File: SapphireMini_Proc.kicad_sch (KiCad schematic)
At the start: 38 parts, among them J801 USB_B_Micro, J802 Conn_02x05_Odd_Even, J803 Conn_02x05_Odd_Even, J805 Conn_01x04_Male, SW801 EVQP7C01P, U801 ATSAMD21G18A-A

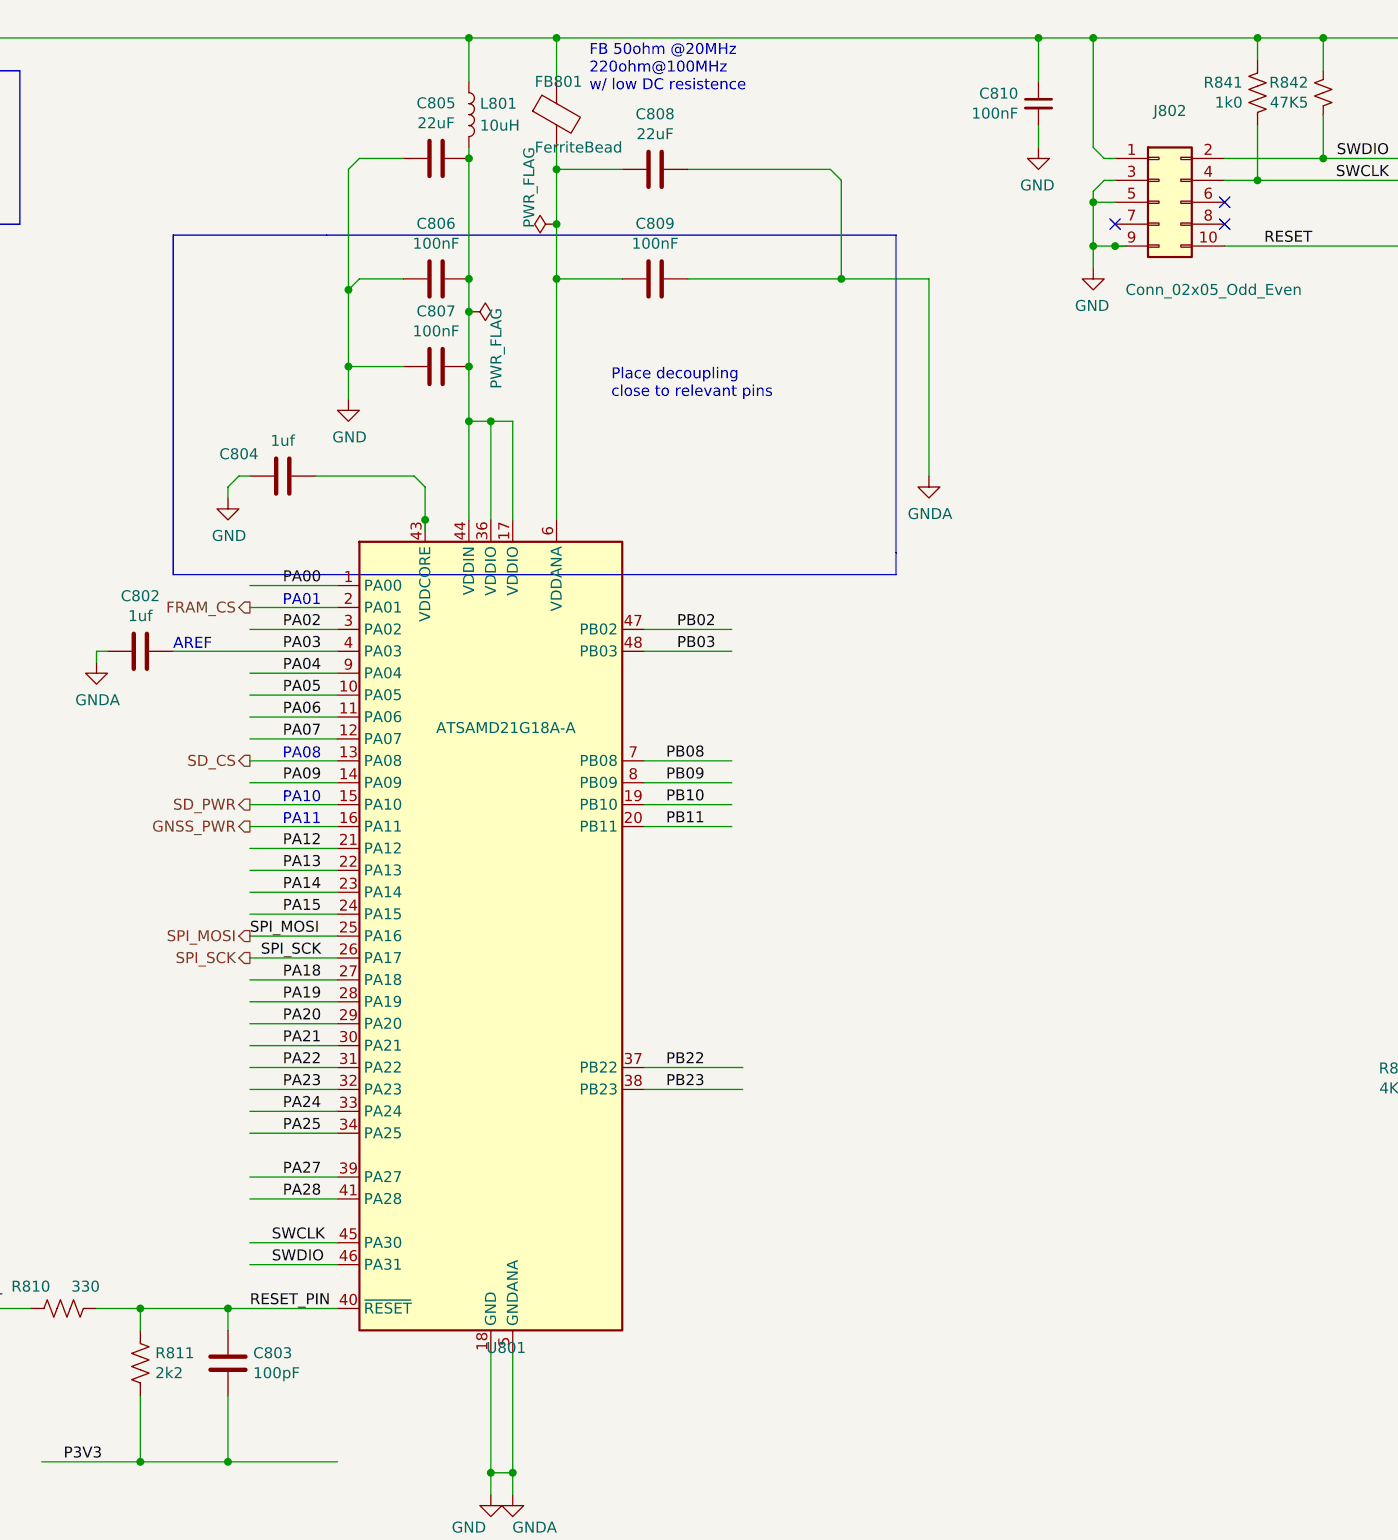
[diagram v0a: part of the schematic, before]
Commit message: Clean PCB but Added new clock to schematic
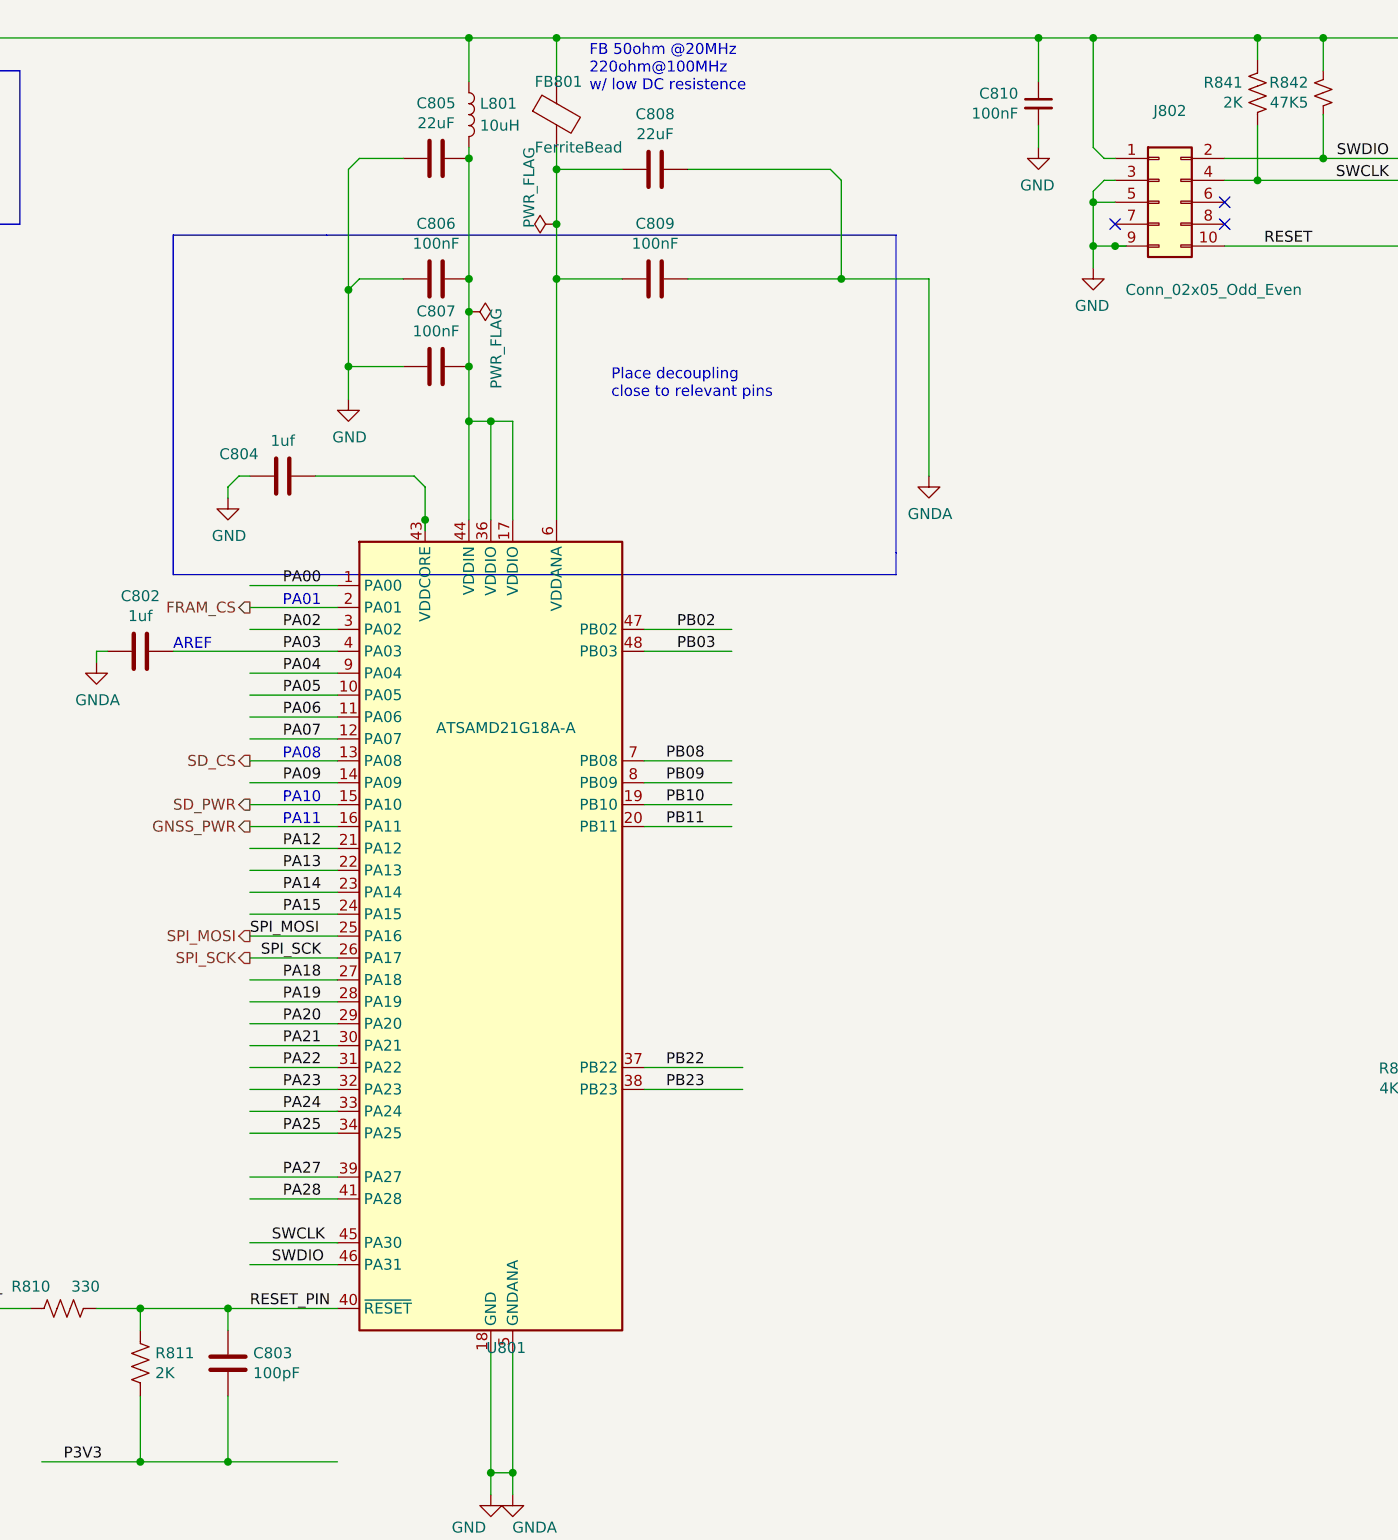
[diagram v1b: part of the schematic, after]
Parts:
- R811: value 2k2 -> 2K; MPN (none) -> CRCW06032K00FKEAC; Manufacturer (none) -> Vishay
- R841: value 1k0 -> 2K; MPN (none) -> CRCW06032K00FKEAC; Manufacturer (none) -> Vishay
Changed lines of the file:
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@@
       (effects (font (size 1.27 1.27)) (justify left))
     )
-    (property "Value" "2k2" (id 1) (at 123.6472 171.323 0)
+    (property "Value" "2K" (id 1) (at 123.6472 171.323 0)
       (effects (font (size 1.27 1.27)) (justify left))
     )
@@
     )
     (property "Datasheet" "~" (id 3) (at 121.92 170.18 0)
+      (effects (font (size 1.27 1.27)) hide)
+    )
+    (property "MPN" "CRCW06032K00FKEAC" (id 4) (at 121.92 170.18 0)
+      (effects (font (size 1.27 1.27)) hide)
+    )
+    (property "Manufacturer" "Vishay" (id 5) (at 121.92 170.18 0)
       (effects (font (size 1.27 1.27)) hide)
     )
@@
       (effects (font (size 1.27 1.27)) (justify left))
     )
-    (property "Value" "1k0" (id 1) (at 249.7328 24.003 0)
+    (property "Value" "2K" (id 1) (at 249.7328 24.003 0)
       (effects (font (size 1.27 1.27)) (justify left))
     )
@@
       (effects (font (size 1.27 1.27)) hide)
     )
+    (property "MPN" "CRCW06032K00FKEAC" (id 4) (at 251.46 22.86 0)
+      (effects (font (size 1.27 1.27)) hide)
+    )
+    (property "Manufacturer" "Vishay" (id 5) (at 251.46 22.86 0)
+      (effects (font (size 1.27 1.27)) hide)
+    )

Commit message: Updating for parts avail
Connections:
- net AUX1: now also R809.4; no longer R812.8
- net PB1: now also R812.5; no longer R809.1
- net RS232_RXD5: now also R812.8; no longer R812.6
- net RS232_TXD5: now also R812.7; no longer R812.5
- net SD_CD: now also R809.1; no longer R812.7
- net VBAT_MON: now also R812.6; no longer R809.4
- net AUX3 renamed CLK_EVI
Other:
- note added: "Attn"
- note added: "Aux Connector"
- note added: "Debug Connector"
- note added: "Processor"
- moved on the sheet: C801, C802, C803, C804, C805, C806, C807, C808, C809, C810, CR801, D801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

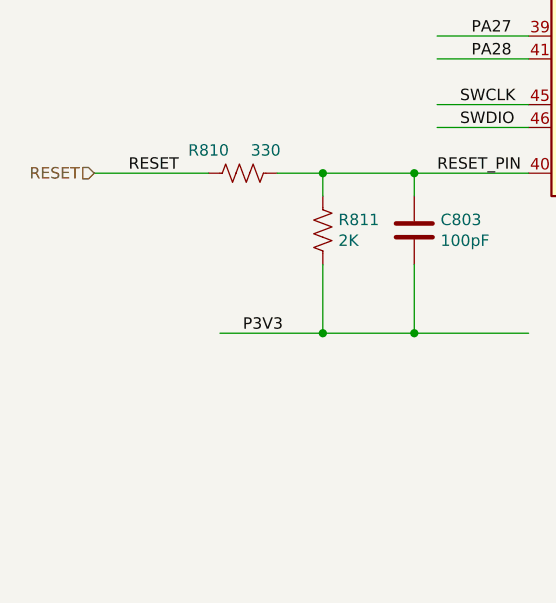
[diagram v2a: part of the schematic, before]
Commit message: Skematic updated for power and 1PSI sensor
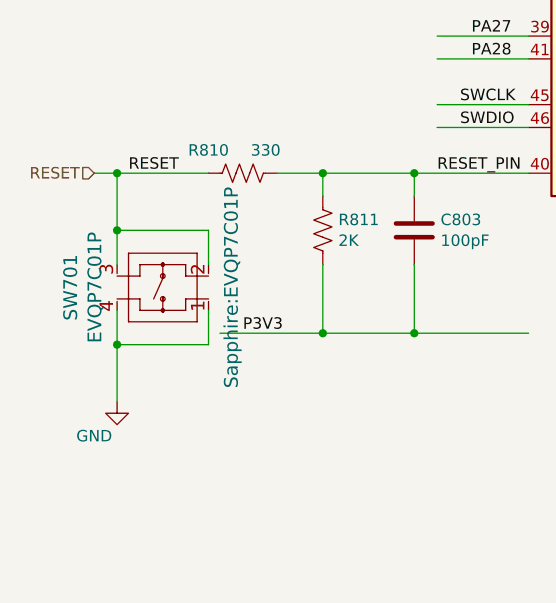
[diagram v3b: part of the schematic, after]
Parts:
- added SW701: EVQP7C01P, Sapphire:EVQP7C01P, symbol EVQP7C01P:EVQP7C01P
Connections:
- net GND: now also SW701.1, SW701.4
- net RESET: now also SW701.2, SW701.3
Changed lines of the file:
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@@
   (junction (at 217.17 81.28) (diameter 0) (color 0 0 0 0)
   )
+  (junction (at 26.67 209.55) (diameter 0) (color 0 0 0 0)
+  )
   (junction (at 49.53 208.28) (diameter 0) (color 0 0 0 0)
   )
@@
   (junction (at 200.66 105.41) (diameter 0) (color 0 0 0 0)
   )
+  (junction (at 26.67 190.5) (diameter 0) (color 0 0 0 0)
+  )
   (junction (at 97.79 64.77) (diameter 0) (color 0 0 0 0)
   )
@@
   (junction (at 90.17 87.63) (diameter 0) (color 0 0 0 0)
   )
+  (junction (at 26.67 196.85) (diameter 0) (color 0 0 0 0)
+  )
   (no_connect (at 241.3 187.96))
   (no_connect (at 213.36 102.87))
@@
     (stroke (width 0) (type default) (color 0 0 0 0))
   )
+  (wire (pts (xy 26.67 200.66) (xy 26.67 196.85))
+    (stroke (width 0) (type default) (color 0 0 0 0))
+  )
   (wire (pts (xy 212.09 193.04) (xy 204.47 193.04))
     (stroke (width 0) (type default) (color 0 0 0 0))
@@
     (stroke (width 0) (type default) (color 0 0 0 0))
   )
+  (wire (pts (xy 36.83 209.55) (xy 26.67 209.55))
+    (stroke (width 0) (type default) (color 0 0 0 0))
+  )
   (wire (pts (xy 59.69 193.04) (xy 59.69 190.5))
     (stroke (width 0) (type default) (color 0 0 0 0))
@@
     (stroke (width 0) (type default) (color 0 0 0 0))
   )
+  (wire (pts (xy 26.67 196.85) (xy 36.83 196.85))
+    (stroke (width 0) (type default) (color 0 0 0 0))
+  )
   (wire (pts (xy 368.3 162.56) (xy 375.92 162.56))
     (stroke (width 0) (type default) (color 0 0 0 0))
@@
     (stroke (width 0) (type default) (color 0 0 0 0))
   )
+  (wire (pts (xy 36.83 205.74) (xy 36.83 209.55))
+    (stroke (width 0) (type default) (color 0 0 0 0))
+  )
   (wire (pts (xy 303.53 118.11) (xy 299.72 118.11))
     (stroke (width 0) (type default) (color 0 0 0 0))
@@
     (stroke (width 0) (type default) (color 0 0 0 0))
   )
+  (wire (pts (xy 36.83 196.85) (xy 36.83 200.66))
+    (stroke (width 0) (type default) (color 0 0 0 0))
+  )
   (wire (pts (xy 283.21 102.87) (xy 270.51 102.87))
     (stroke (width 0) (type default) (color 0 0 0 0))
@@
     (stroke (width 0) (type default) (color 0 0 0 0))
   )
+  (wire (pts (xy 26.67 190.5) (xy 24.13 190.5))
+    (stroke (width 0) (type default) (color 0 0 0 0))
+  )
   (wire (pts (xy 130.81 71.12) (xy 140.97 71.12))
     (stroke (width 0) (type default) (color 0 0 0 0))
@@
     (stroke (width 0) (type default) (color 0 0 0 0))
   )
+  (wire (pts (xy 26.67 209.55) (xy 26.67 215.9))
+    (stroke (width 0) (type default) (color 0 0 0 0))
+  )
   (wire (pts (xy 369.57 57.15) (xy 375.92 57.15))
     (stroke (width 0) (type default) (color 0 0 0 0))
@@
     (stroke (width 0) (type default) (color 0 0 0 0))
   )
+  (wire (pts (xy 26.67 196.85) (xy 26.67 190.5))
+    (stroke (width 0) (type default) (color 0 0 0 0))
+  )
   (wire (pts (xy 59.69 96.52) (xy 59.69 95.25))
     (stroke (width 0) (type default) (color 0 0 0 0))
@@
     (stroke (width 0) (type default) (color 0 0 0 0))
   )
-  (wire (pts (xy 36.83 190.5) (xy 24.13 190.5))
+  (wire (pts (xy 36.83 190.5) (xy 26.67 190.5))
     (stroke (width 0) (type default) (color 0 0 0 0))
   )
@@
     (stroke (width 0) (type default) (color 0 0 0 0))
   )
+  (wire (pts (xy 26.67 205.74) (xy 26.67 209.55))
+    (stroke (width 0) (type default) (color 0 0 0 0))
+  )
   (wire (pts (xy 369.57 62.23) (xy 375.92 62.23))
     (stroke (width 0) (type default) (color 0 0 0 0))
@@
     (pin "4")
   )
+  (symbol (lib_id "EVQP7C01P:EVQP7C01P") (at 33.02 229.87 90) (unit 1)
+    (in_bom yes) (on_board yes)
+    (property "Reference" "SW701" (id 0) (at 21.5138 203.2 0)
+      (effects (font (size 1.524 1.524)))
+    )
+    (property "Value" "EVQP7C01P" (id 1) (at 24.2062 203.2 0)
+      (effects (font (size 1.524 1.524)))
+    )
+    (property "Footprint" "Sapphire:EVQP7C01P" (id 2) (at 39.37 203.2 0)
+      (effects (font (size 1.524 1.524)))
+    )
+    (property "Datasheet" "" (id 3) (at 33.02 229.87 0)
+      (effects (font (size 1.524 1.524)))
+    )
+    (property "Populate" "1" (id 4) (at 33.02 229.87 0)
+      (effects (font (size 1.27 1.27)) hide)
+    )
+    (property "Description" "Tactile Switch SPST-NO Side Actuated Surface Mount, Right Angle" (id 5) (at 33.02 229.87 0)
+      (effects (font (size 1.27 1.27)) hide)
+    )
+    (property "Digi-Key_PN" "P16765CT-ND" (id 6) (at 33.02 229.87 0)
+      (effects (font (size 1.27 1.27)) hide)
+    )
+    (property "MPN" "EVQ-P7C01P" (id 7) (at 33.02 229.87 0)
+      (effects (font (size 1.27 1.27)) hide)
+    )
+    (property "Distributor" "Digikey" (id 8) (at 33.02 229.87 0)
+      (effects (font (size 1.27 1.27)) hide)
+    )
+    (pin "1")
+    (pin "2")
+    (pin "3")
+    (pin "4")
+  )
   (symbol (lib_id "PanasonicRA:EXB-2HV470JV") (at 355.6 127 0) (unit 1)
     (in_bom yes) (on_board yes)
@@
       (effects (font (size 1.27 1.27)) hide)
     )
+    (pin "1")
+  )
+  (symbol (lib_id "power:GND") (at 26.67 215.9 0) (unit 1)
+    (in_bom yes) (on_board yes)
+    (property "Reference" "#PWR0105" (id 0) (at 26.67 222.25 0)
+      (effects (font (size 1.27 1.27)) hide)
+    )
+    (property "Value" "GND" (id 1) (at 24.13 219.71 0))
+    (property "Footprint" "" (id 2) (at 26.67 215.9 0)
+      (effects (font (size 1.27 1.27)) hide)
+    )
+    (property "Datasheet" "" (id 3) (at 26.67 215.9 0)
+      (effects (font (size 1.27 1.27)) hide)
+    )
